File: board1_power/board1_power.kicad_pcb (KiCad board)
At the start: 4 copper layers, 100 x 100 mm, 145 parts, among them J1 Conn_02x04_Odd_Even, J2 Conn_01x04, J3 USB_C_Receptacle_USB2.0_16P, J4 POWER_OFF_HEADER, J5 BH-18650-A1BJ024, Q1 DMG2305UX, Q2 SI4920DY, Q3 DMG2305UX, Q4 SI4920DY, Q5 DMG2305UX, Q6 SI4920DY, Q7 DMG2305UX, Q8 SI4920DY, Q9 2N7002, U1 ESP32-S3-WROOM-1, U10 SY6970QCC, U11 DW01A, U12 SY6970QCC, U13 DW01A, U2 TCA9548APWR, U3 AP2112K-3.3, U4 USBLC6-2SC6, U5 CH224K, U6 SY6970QCC, U7 DW01A, U8 SY6970QCC, U9 DW01A

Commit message: connector fixes to the boards - swapped headers with sockets and vice versa. had to adjust the schematics too but no big changes, everything still connected appropriately
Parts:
- J1: footprint Connector_PinHeader_2.54mm:PinHeader_2x04_P2.54mm_Horizontal -> Connector_PinSocket_2.54mm:PinSocket_2x04_P2.54mm_Horizontal
- J2: footprint Connector_PinHeader_2.54mm:PinHeader_1x04_P2.54mm_Horizontal -> Connector_PinSocket_2.54mm:PinSocket_1x04_P2.54mm_Horizontal
- moved J1 7.62 mm to (251.3, 32.1), turned to -90 degrees
- moved J2 7.62 mm to (238.7, 29.6), turned to -90 degrees
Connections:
- J1 pad 1: /CH4_V -> /CH1_V
- J1 pad 3: /CH3_V -> /CH2_V
- J1 pad 5: /CH2_V -> /CH3_V
- J1 pad 7: /CH1_V -> /CH4_V
- J2 pad 1: SDA -> GND
- J2 pad 2: SCL -> /WAKE
- J2 pad 3: /WAKE -> SCL
- J2 pad 4: GND -> SDA
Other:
- board text added: "4 INDEPENDENT CELL 18650 CELL CHARGER"
- board text removed: "4 INDIPENDENT CELL 18650 CELL CHARGER"

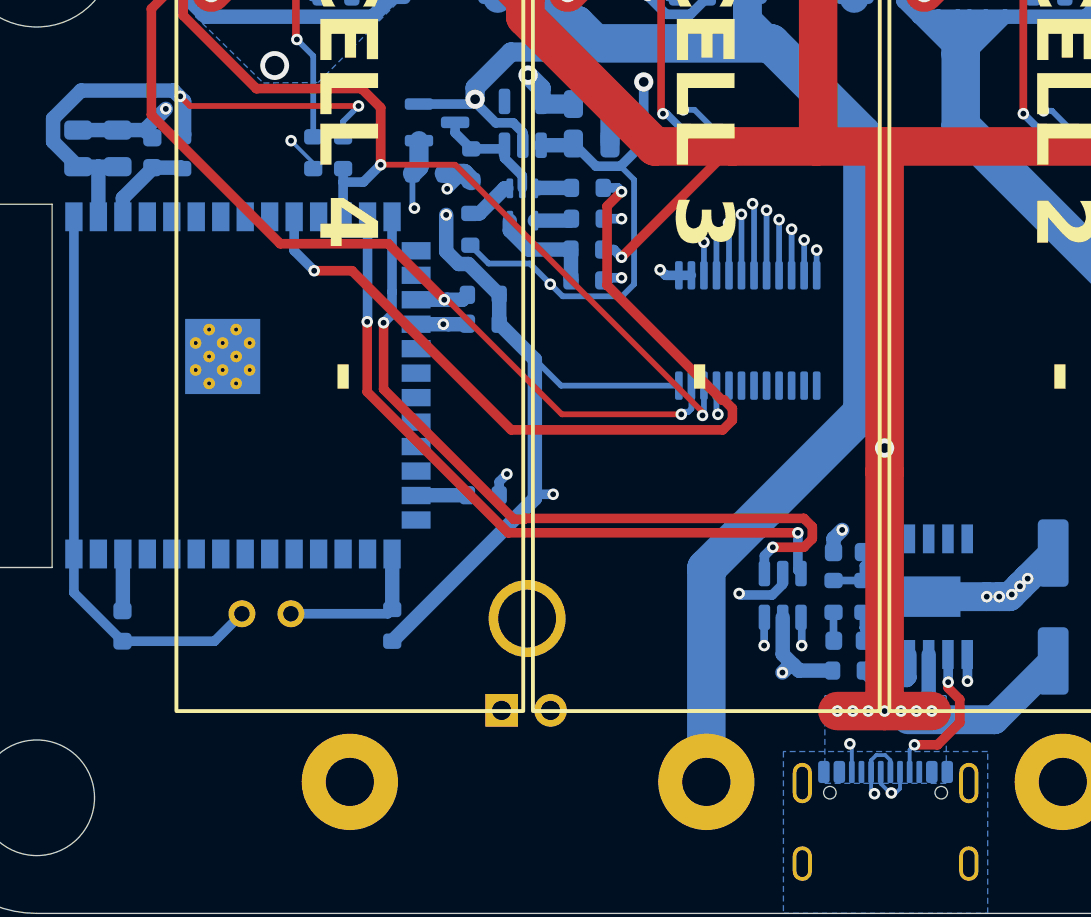
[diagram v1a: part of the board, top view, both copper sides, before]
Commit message: board1_power: fix PD straps + heartbeat LED resistor
- CH224K now deterministically 12V: CFG1->GND (0R), CFG2->GND (0R),
  CFG3->VDD_PD (10k pull-up = logic 1). Previously CFG2/CFG3 floated.
- Heartbeat LED D1 now has 330R series resistor to IO2 (was direct
  GPIO->LED->GND).

Closes the two items in docs/board1_fixes_todo.md.
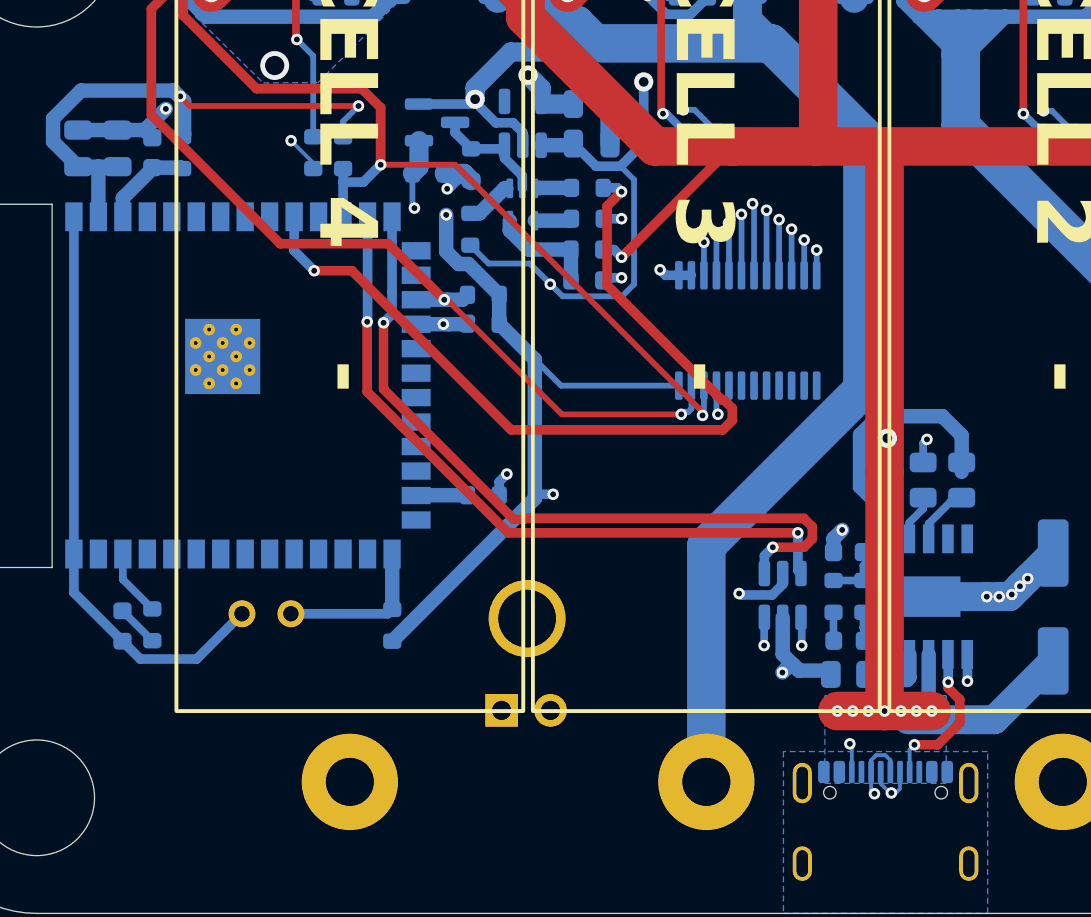
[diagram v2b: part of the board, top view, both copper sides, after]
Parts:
- added R55: 0R, Resistor_SMD:R_0805_2012Metric, B.Cu at (228.8, 94.4)
- added R62: 10k, Resistor_SMD:R_0805_2012Metric, B.Cu at (230.8, 94.4)
- added R8: 330R, Resistor_SMD:R_0603_1608Metric, B.Cu at (188.8, 101.9)
- R11: value 24K -> 0R; footprint Resistor_SMD:R_0603_1608Metric -> Resistor_SMD:R_0805_2012Metric
- moved R12 0.49 mm to (226.8, 94.4)
- moved R11 0.20 mm to (224.9, 104.5)
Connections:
- D1 pad 2: /Heartbeat LED -> Net-(D1-A)
- U5 pad 2: unconnected-(U5-CFG2-Pad2) -> Net-(U5-CFG2)
- U5 pad 3: unconnected-(U5-CFG3-Pad3) -> Net-(U5-CFG3)
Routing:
- net /USB_IN/VDD_PD: track 6.76 -> 19.9 mm
- net Net-(U5-CFG3): track 0.00 -> 2.98 mm
- net Net-(U5-CFG2): track 0.00 -> 2.43 mm
- net Net-(D1-A): track 0.00 -> 2.22 mm
- net GND: track 254.3 -> 256.4 mm, vias 44 -> 45
- net /Heartbeat LED: track 2.96 -> 3.48 mm
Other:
- board text added: "HB"
